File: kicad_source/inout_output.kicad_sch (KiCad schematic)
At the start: 8 parts

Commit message: started layout
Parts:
- gave numbers to parts that had none: 8
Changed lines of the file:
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@@
   (symbol (lib_id "power:GND") (at 85.09 71.12 0) (unit 1)
     (in_bom yes) (on_board yes) (fields_autoplaced)
-    (property "Reference" "#PWR?" (id 0) (at 85.09 77.47 0)
+    (property "Reference" "#PWR0124" (id 0) (at 85.09 77.47 0)
       (effects (font (size 1.27 1.27)) hide)
     )
@@
   (symbol (lib_id "power:GND") (at 140.97 113.03 0) (unit 1)
     (in_bom yes) (on_board yes) (fields_autoplaced)
-    (property "Reference" "#PWR?" (id 0) (at 140.97 119.38 0)
+    (property "Reference" "#PWR0133" (id 0) (at 140.97 119.38 0)
       (effects (font (size 1.27 1.27)) hide)
     )
@@
   (symbol (lib_id "power:GND") (at 119.38 97.79 0) (unit 1)
     (in_bom yes) (on_board yes) (fields_autoplaced)
-    (property "Reference" "#PWR?" (id 0) (at 119.38 104.14 0)
+    (property "Reference" "#PWR0131" (id 0) (at 119.38 104.14 0)
       (effects (font (size 1.27 1.27)) hide)
     )
@@
   (symbol (lib_id "power:GND") (at 119.38 52.07 0) (unit 1)
     (in_bom yes) (on_board yes) (fields_autoplaced)
-    (property "Reference" "#PWR?" (id 0) (at 119.38 58.42 0)
+    (property "Reference" "#PWR0129" (id 0) (at 119.38 58.42 0)
       (effects (font (size 1.27 1.27)) hide)
     )
@@
   (symbol (lib_id "power:GND") (at 140.97 67.31 0) (unit 1)
     (in_bom yes) (on_board yes) (fields_autoplaced)
-    (property "Reference" "#PWR?" (id 0) (at 140.97 73.66 0)
+    (property "Reference" "#PWR0132" (id 0) (at 140.97 73.66 0)
       (effects (font (size 1.27 1.27)) hide)
     )
@@
   (symbol (lib_id "power:+BATT") (at 119.38 43.18 0) (unit 1)
     (in_bom yes) (on_board yes) (fields_autoplaced)
-    (property "Reference" "#PWR?" (id 0) (at 119.38 46.99 0)
+    (property "Reference" "#PWR0128" (id 0) (at 119.38 46.99 0)
       (effects (font (size 1.27 1.27)) hide)
     )
@@
   (symbol (lib_id "Device:R_Small") (at 85.09 67.31 0) (unit 1)
     (in_bom yes) (on_board yes) (fields_autoplaced)
-    (property "Reference" "R?" (id 0) (at 87.63 66.0399 0)
+    (property "Reference" "R46" (id 0) (at 87.63 66.0399 0)
       (effects (font (size 1.27 1.27)) (justify left))
     )
@@
   (symbol (lib_id "generationmake:ITS4200S-ME-P") (at 105.41 107.95 0) (unit 1)
     (in_bom yes) (on_board yes) (fields_autoplaced)
-    (property "Reference" "U?" (id 0) (at 106.045 96.52 0))
+    (property "Reference" "U15" (id 0) (at 106.045 96.52 0))
     (property "Value" "ITS4200S-ME-P" (id 1) (at 106.045 99.06 0))
     (property "Footprint" "Package_TO_SOT_SMD:SOT-223" (id 2) (at 105.41 107.95 0)
@@
   (symbol (lib_id "generationmake:ITS4200S-ME-P") (at 105.41 62.23 0) (unit 1)
     (in_bom yes) (on_board yes) (fields_autoplaced)
-    (property "Reference" "U?" (id 0) (at 106.045 50.8 0))
+    (property "Reference" "U14" (id 0) (at 106.045 50.8 0))
     (property "Value" "ITS4200S-ME-P" (id 1) (at 106.045 53.34 0))
     (property "Footprint" "Package_TO_SOT_SMD:SOT-223" (id 2) (at 105.41 62.23 0)
@@
   (symbol (lib_id "Device:R_Small") (at 85.09 113.03 0) (unit 1)
     (in_bom yes) (on_board yes) (fields_autoplaced)
-    (property "Reference" "R?" (id 0) (at 87.63 111.7599 0)
+    (property "Reference" "R47" (id 0) (at 87.63 111.7599 0)
       (effects (font (size 1.27 1.27)) (justify left))
     )
@@
   (symbol (lib_id "power:GND") (at 85.09 116.84 0) (unit 1)
     (in_bom yes) (on_board yes) (fields_autoplaced)
-    (property "Reference" "#PWR?" (id 0) (at 85.09 123.19 0)
+    (property "Reference" "#PWR0125" (id 0) (at 85.09 123.19 0)
       (effects (font (size 1.27 1.27)) hide)
     )
@@
   (symbol (lib_id "power:GND") (at 115.57 69.85 0) (unit 1)
     (in_bom yes) (on_board yes) (fields_autoplaced)
-    (property "Reference" "#PWR?" (id 0) (at 115.57 76.2 0)
+    (property "Reference" "#PWR0126" (id 0) (at 115.57 76.2 0)
       (effects (font (size 1.27 1.27)) hide)
     )
@@
   (symbol (lib_id "power:GND") (at 115.57 115.57 0) (unit 1)
     (in_bom yes) (on_board yes) (fields_autoplaced)
-    (property "Reference" "#PWR?" (id 0) (at 115.57 121.92 0)
+    (property "Reference" "#PWR0127" (id 0) (at 115.57 121.92 0)
       (effects (font (size 1.27 1.27)) hide)
     )
@@
   (symbol (lib_id "Device:C_Small") (at 119.38 48.26 0) (unit 1)
     (in_bom yes) (on_board yes) (fields_autoplaced)
-    (property "Reference" "C?" (id 0) (at 121.92 46.9962 0)
+    (property "Reference" "C46" (id 0) (at 121.92 46.9962 0)
       (effects (font (size 1.27 1.27)) (justify left))
     )
@@
   (symbol (lib_id "Connector_Generic:Conn_01x02") (at 148.59 107.95 0) (unit 1)
     (in_bom yes) (on_board yes) (fields_autoplaced)
-    (property "Reference" "J?" (id 0) (at 151.13 107.9499 0)
+    (property "Reference" "J14" (id 0) (at 151.13 107.9499 0)
       (effects (font (size 1.27 1.27)) (justify left))
     )
@@
   (symbol (lib_id "power:+BATT") (at 119.38 88.9 0) (unit 1)
     (in_bom yes) (on_board yes) (fields_autoplaced)
-    (property "Reference" "#PWR?" (id 0) (at 119.38 92.71 0)
+    (property "Reference" "#PWR0130" (id 0) (at 119.38 92.71 0)
       (effects (font (size 1.27 1.27)) hide)
     )
@@
   (symbol (lib_id "Connector_Generic:Conn_01x02") (at 148.59 62.23 0) (unit 1)
     (in_bom yes) (on_board yes) (fields_autoplaced)
-    (property "Reference" "J?" (id 0) (at 151.13 62.2299 0)
+    (property "Reference" "J13" (id 0) (at 151.13 62.2299 0)
       (effects (font (size 1.27 1.27)) (justify left))
     )
@@
   (symbol (lib_id "Device:C_Small") (at 119.38 93.98 0) (unit 1)
     (in_bom yes) (on_board yes) (fields_autoplaced)
-    (property "Reference" "C?" (id 0) (at 121.92 92.7162 0)
-      (effects (font (size 1.27 1.27)) (justify left))
-    )
+    (property "Reference" "C47" (id 0) (at 121.92 92.7162 0)
+      (effects (font (size 1.27 1.27)) (justify left))
+    )

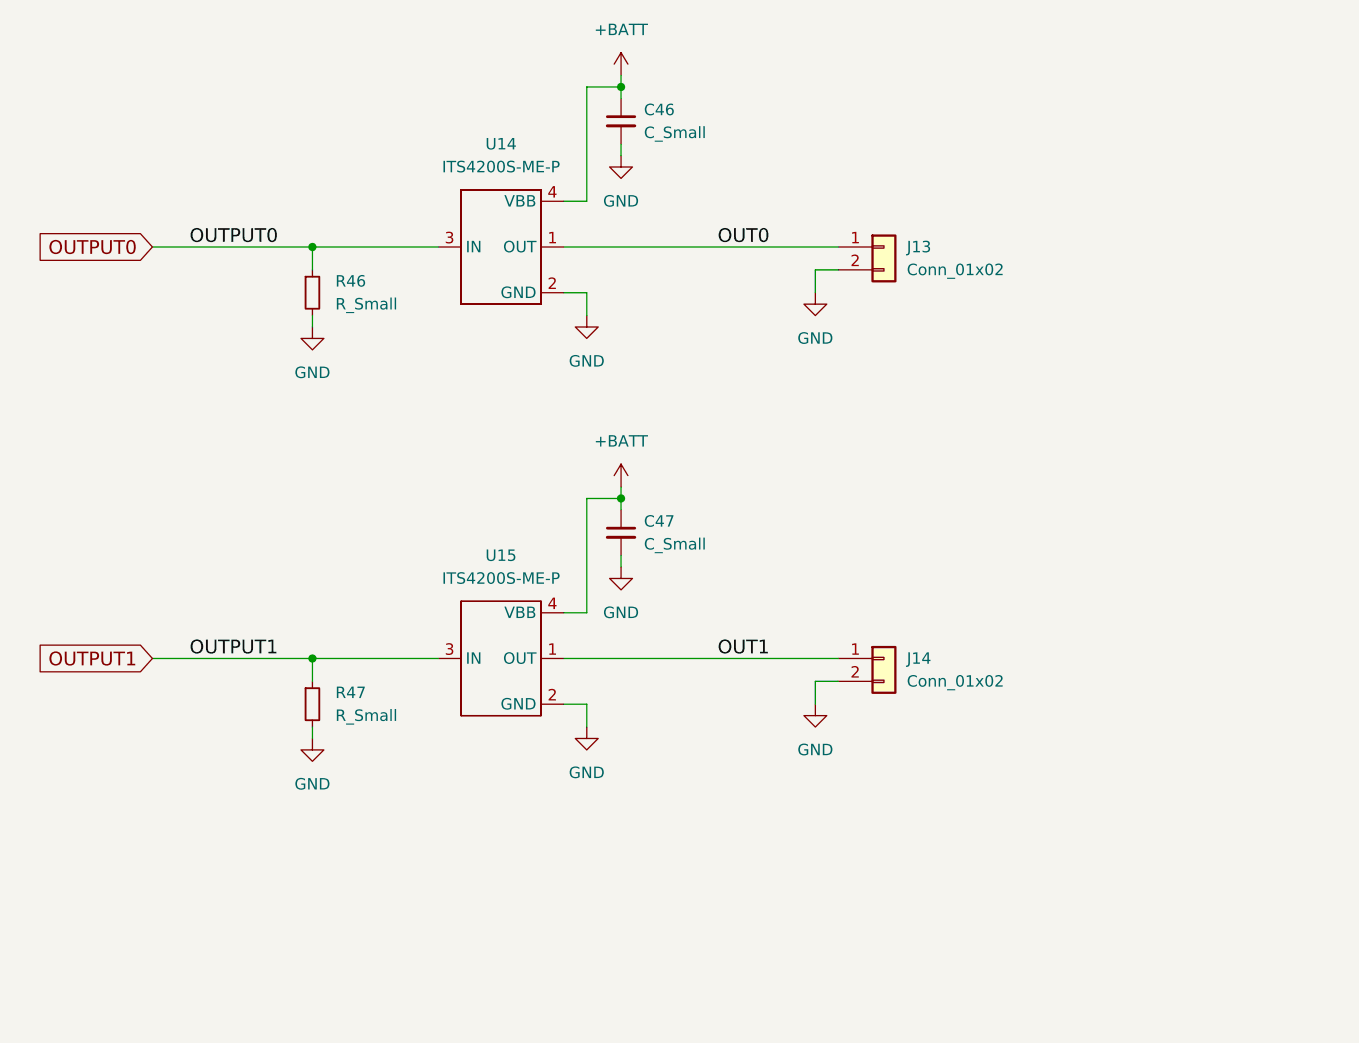
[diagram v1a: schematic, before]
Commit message: updated schematic pdf
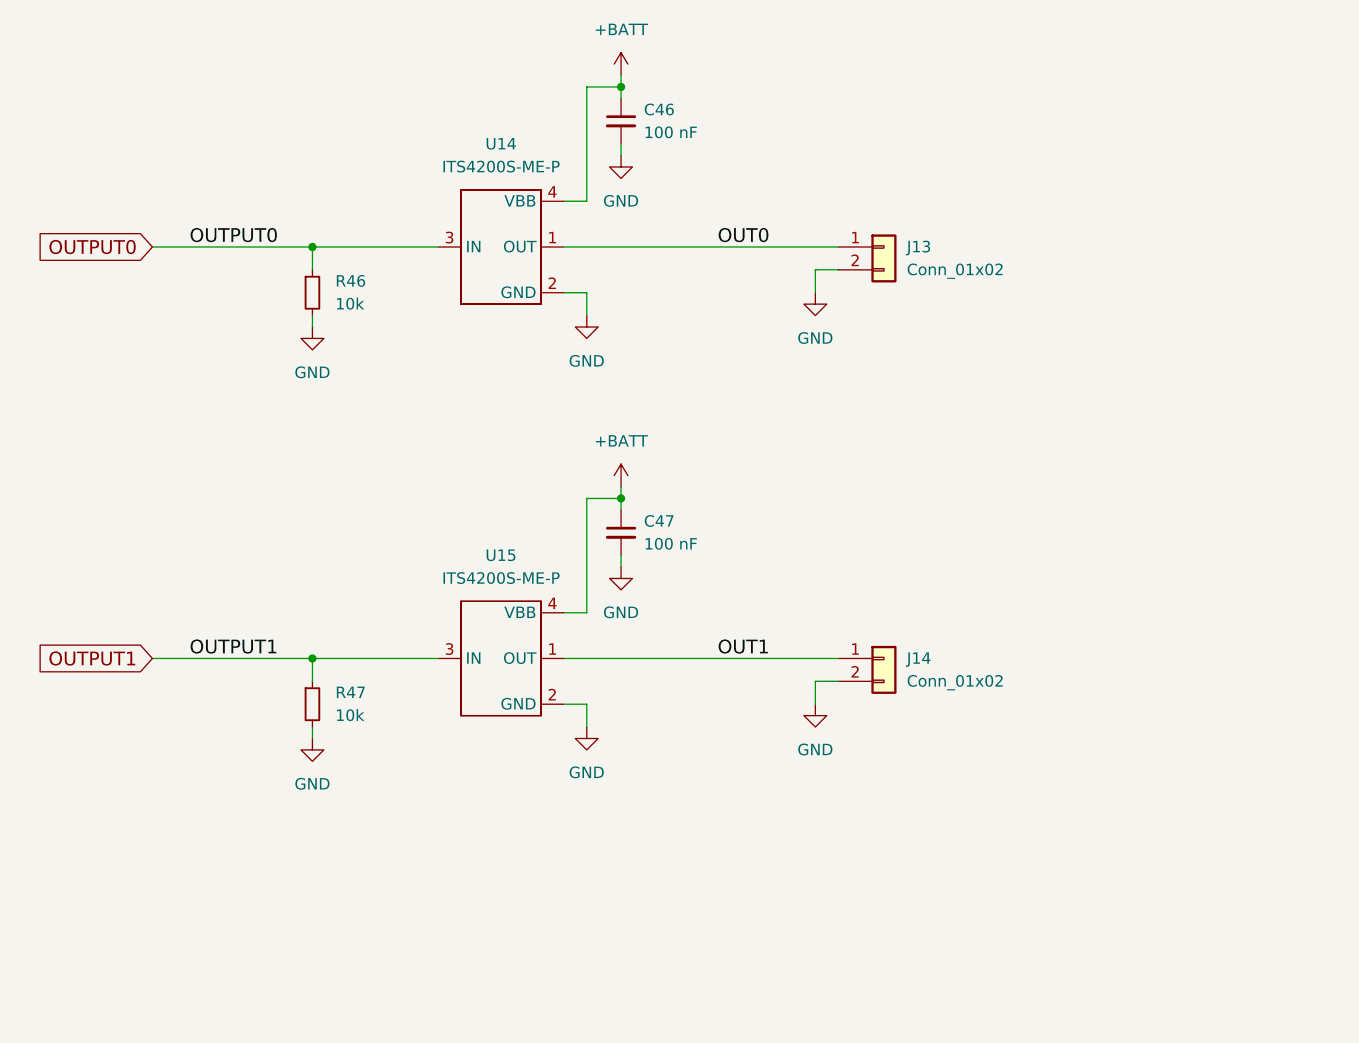
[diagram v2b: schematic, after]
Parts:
- C46, C47: value C_Small -> 100 nF
- R46, R47: value R_Small -> 10k
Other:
- company: (none) -> generationmake
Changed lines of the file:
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@@
   (title_block
     (title "CyphalRobotController07/CAN")
-    (date "2023-10-01")
+    (date "2023-10-02")
     (rev "0.1")
+    (company "generationmake")
   )
   (junction (at 85.09 62.23) (diameter 0) (color 0 0 0 0)
@@
       (effects (font (size 1.27 1.27)) (justify left))
     )
-    (property "Value" "R_Small" (id 1) (at 87.63 68.5799 0)
+    (property "Value" "10k" (id 1) (at 87.63 68.5799 0)
       (effects (font (size 1.27 1.27)) (justify left))
     )
@@
       (effects (font (size 1.27 1.27)) (justify left))
     )
-    (property "Value" "R_Small" (id 1) (at 87.63 114.2999 0)
+    (property "Value" "10k" (id 1) (at 87.63 114.2999 0)
       (effects (font (size 1.27 1.27)) (justify left))
     )
@@
       (effects (font (size 1.27 1.27)) (justify left))
     )
-    (property "Value" "C_Small" (id 1) (at 121.92 49.5362 0)
+    (property "Value" "100 nF" (id 1) (at 121.92 49.5362 0)
       (effects (font (size 1.27 1.27)) (justify left))
     )
@@
       (effects (font (size 1.27 1.27)) (justify left))
     )
-    (property "Value" "C_Small" (id 1) (at 121.92 95.2562 0)
-      (effects (font (size 1.27 1.27)) (justify left))
-    )
+    (property "Value" "100 nF" (id 1) (at 121.92 95.2562 0)
+      (effects (font (size 1.27 1.27)) (justify left))
+    )

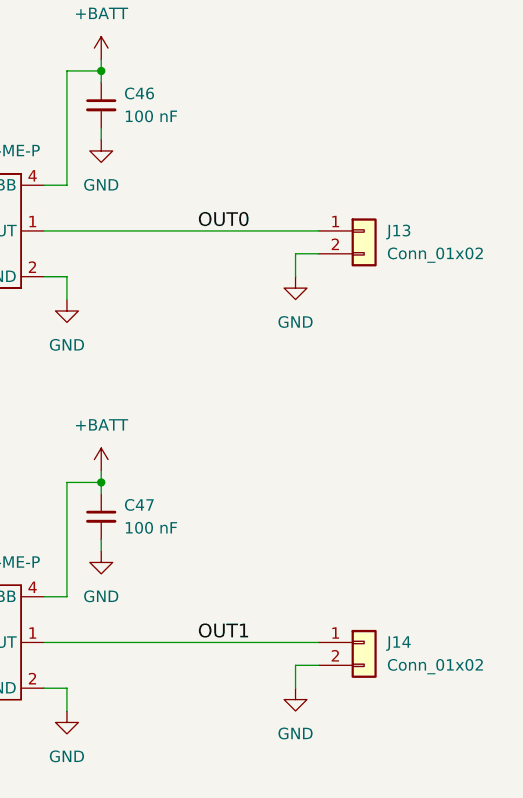
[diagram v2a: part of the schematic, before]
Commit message: updated 3d model to fit to reality
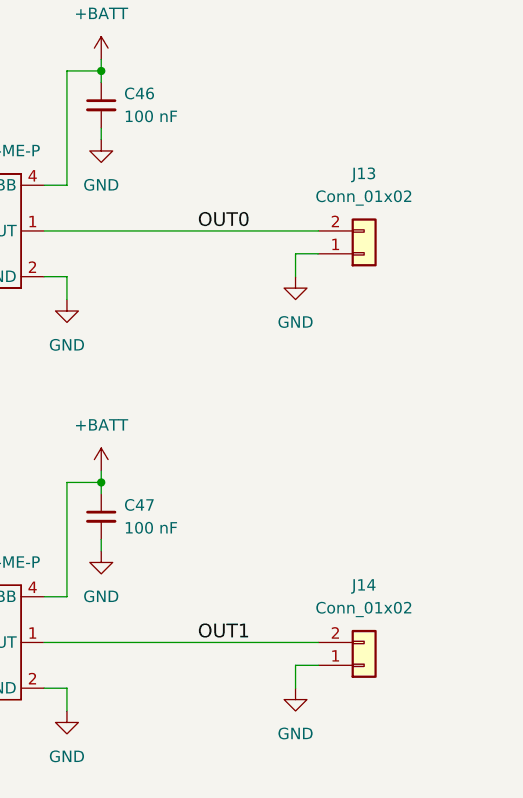
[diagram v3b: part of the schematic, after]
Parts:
- J13, J14: footprint Connector_Phoenix_MC:PhoenixContact_MCV_1,5_2-G-3.81_1x02_P3.81mm_Vertical -> Connector_Phoenix_MC:PhoenixContact_MC_1,5_2-G-3.81_1x02_P3.81mm_Horizontal
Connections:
- net GND: now also J13.1 (Pin_1), J14.1 (Pin_1); no longer J13.2 (Pin_2), J14.2 (Pin_2)
- net OUT0: now also J13.2 (Pin_2); no longer J13.1 (Pin_1)
- net OUT1: now also J14.2 (Pin_2); no longer J14.1 (Pin_1)
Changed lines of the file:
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@@
   (title_block
     (title "CyphalRobotController07/CAN")
-    (date "2023-10-02")
+    (date "2023-11-15")
     (rev "0.1")
     (company "generationmake")
@@
     (pin "2")
   )
-  (symbol (lib_id "Connector_Generic:Conn_01x02") (at 148.59 107.95 0) (unit 1)
-    (in_bom yes) (on_board yes) (fields_autoplaced)
-    (property "Reference" "J14" (id 0) (at 151.13 107.9499 0)
-      (effects (font (size 1.27 1.27)) (justify left))
-    )
-    (property "Value" "Conn_01x02" (id 1) (at 151.13 110.4899 0)
-      (effects (font (size 1.27 1.27)) (justify left))
-    )
-    (property "Footprint" "Connector_Phoenix_MC:PhoenixContact_MCV_1,5_2-G-3.81_1x02_P3.81mm_Vertical" (id 2) (at 148.59 107.95 0)
-      (effects (font (size 1.27 1.27)) hide)
-    )
-    (property "Datasheet" "~" (id 3) (at 148.59 107.95 0)
+  (symbol (lib_id "Connector_Generic:Conn_01x02") (at 148.59 110.49 0) (mirror x) (unit 1)
+    (in_bom yes) (on_board yes) (fields_autoplaced)
+    (property "Reference" "J14" (id 0) (at 148.59 101.6 0))
+    (property "Value" "Conn_01x02" (id 1) (at 148.59 104.14 0))
+    (property "Footprint" "Connector_Phoenix_MC:PhoenixContact_MC_1,5_2-G-3.81_1x02_P3.81mm_Horizontal" (id 2) (at 148.59 110.49 0)
+      (effects (font (size 1.27 1.27)) hide)
+    )
+    (property "Datasheet" "~" (id 3) (at 148.59 110.49 0)
       (effects (font (size 1.27 1.27)) hide)
     )
@@
     (pin "1")
   )
-  (symbol (lib_id "Connector_Generic:Conn_01x02") (at 148.59 62.23 0) (unit 1)
-    (in_bom yes) (on_board yes) (fields_autoplaced)
-    (property "Reference" "J13" (id 0) (at 151.13 62.2299 0)
-      (effects (font (size 1.27 1.27)) (justify left))
-    )
-    (property "Value" "Conn_01x02" (id 1) (at 151.13 64.7699 0)
-      (effects (font (size 1.27 1.27)) (justify left))
-    )
-    (property "Footprint" "Connector_Phoenix_MC:PhoenixContact_MCV_1,5_2-G-3.81_1x02_P3.81mm_Vertical" (id 2) (at 148.59 62.23 0)
-      (effects (font (size 1.27 1.27)) hide)
-    )
-    (property "Datasheet" "~" (id 3) (at 148.59 62.23 0)
-      (effects (font (size 1.27 1.27)) hide)
-    )
+  (symbol (lib_id "Connector_Generic:Conn_01x02") (at 148.59 64.77 0) (mirror x) (unit 1)
+    (in_bom yes) (on_board yes) (fields_autoplaced)
+    (property "Reference" "J13" (id 0) (at 148.59 55.88 0))
+    (property "Value" "Conn_01x02" (id 1) (at 148.59 58.42 0))
+    (property "Footprint" "Connector_Phoenix_MC:PhoenixContact_MC_1,5_2-G-3.81_1x02_P3.81mm_Horizontal" (id 2) (at 148.59 64.77 0)
+      (effects (font (size 1.27 1.27)) hide)
+    )
+    (property "Datasheet" "~" (id 3) (at 148.59 64.77 0)
+      (effects (font (size 1.27 1.27)) hide)
+    )

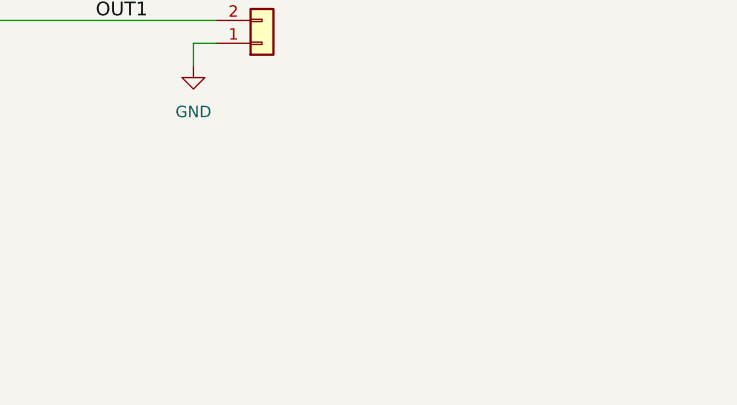
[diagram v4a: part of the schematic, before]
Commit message: added always on connector for +BATT
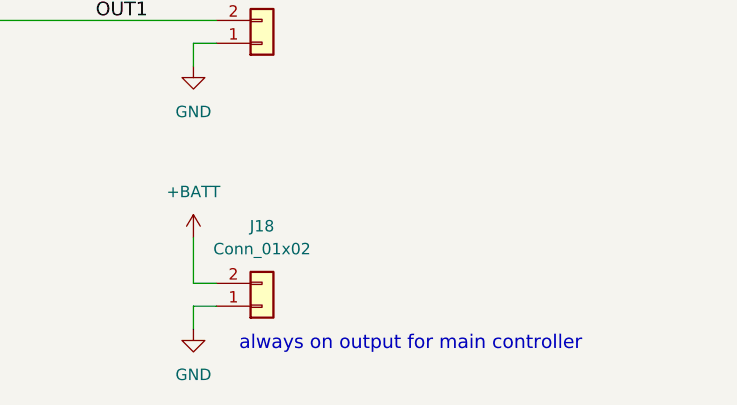
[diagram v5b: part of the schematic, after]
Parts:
- added J18: Conn_01x02, Connector_Phoenix_MC:PhoenixContact_MC_1,5_2-G-3.81_1x02_P3.81mm_Horizontal, symbol Connector_Generic:Conn_01x02
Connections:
- net +BATT: now also J18.2 (Pin_2)
- net GND: now also J18.1 (Pin_1)
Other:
- note added: "always on output for main controller"
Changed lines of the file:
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@@
+    (stroke (width 0) (type default) (color 0 0 0 0))
+  )
+  (wire (pts (xy 140.97 137.16) (xy 143.51 137.16))
     (stroke (width 0) (type default) (color 0 0 0 0))
   )
@@
     (stroke (width 0) (type default) (color 0 0 0 0))
   )
+  (wire (pts (xy 140.97 132.08) (xy 140.97 137.16))
+    (stroke (width 0) (type default) (color 0 0 0 0))
+  )
   (wire (pts (xy 67.31 62.23) (xy 85.09 62.23))
     (stroke (width 0) (type default) (color 0 0 0 0))
@@
     (stroke (width 0) (type default) (color 0 0 0 0))
   )
+  (wire (pts (xy 143.51 139.7) (xy 140.97 139.7))
+    (stroke (width 0) (type default) (color 0 0 0 0))
+  )
   (wire (pts (xy 115.57 57.15) (xy 115.57 44.45))
     (stroke (width 0) (type default) (color 0 0 0 0))
@@
     (stroke (width 0) (type default) (color 0 0 0 0))
   )
+  (wire (pts (xy 140.97 139.7) (xy 140.97 142.24))
+    (stroke (width 0) (type default) (color 0 0 0 0))
+  )
   (wire (pts (xy 119.38 88.9) (xy 119.38 90.17))
     (stroke (width 0) (type default) (color 0 0 0 0))
@@
   (wire (pts (xy 113.03 102.87) (xy 115.57 102.87))
     (stroke (width 0) (type default) (color 0 0 0 0))
+  )
+  (text "always on output for main controller" (at 146.05 144.78 0)
+    (effects (font (size 1.524 1.524)) (justify left bottom))
   )
   (label "OUT1" (at 135.89 107.95 180)
@@
     )
   )
+  (symbol (lib_id "power:+BATT") (at 140.97 132.08 0) (unit 1)
+    (in_bom yes) (on_board yes) (fields_autoplaced)
+    (property "Reference" "#PWR0160" (id 0) (at 140.97 135.89 0)
+      (effects (font (size 1.27 1.27)) hide)
+    )
+    (property "Value" "+BATT" (id 1) (at 140.97 127 0))
+    (property "Footprint" "" (id 2) (at 140.97 132.08 0)
+      (effects (font (size 1.27 1.27)) hide)
+    )
+    (property "Datasheet" "" (id 3) (at 140.97 132.08 0)
+      (effects (font (size 1.27 1.27)) hide)
+    )
+    (pin "1")
+  )
   (symbol (lib_id "power:GND") (at 85.09 71.12 0) (unit 1)
     (in_bom yes) (on_board yes) (fields_autoplaced)
@@
     (pin "1")
   )
+  (symbol (lib_id "power:GND") (at 140.97 142.24 0) (unit 1)
+    (in_bom yes) (on_board yes) (fields_autoplaced)
+    (property "Reference" "#PWR0161" (id 0) (at 140.97 148.59 0)
+      (effects (font (size 1.27 1.27)) hide)
+    )
+    (property "Value" "GND" (id 1) (at 140.97 147.32 0))
+    (property "Footprint" "" (id 2) (at 140.97 142.24 0)
+      (effects (font (size 1.27 1.27)) hide)
+    )
+    (property "Datasheet" "" (id 3) (at 140.97 142.24 0)
+      (effects (font (size 1.27 1.27)) hide)
+    )
+    (pin "1")
+  )
+  (symbol (lib_id "Connector_Generic:Conn_01x02") (at 148.59 139.7 0) (mirror x) (unit 1)
+    (in_bom yes) (on_board yes) (fields_autoplaced)
+    (property "Reference" "J18" (id 0) (at 148.59 130.81 0))
+    (property "Value" "Conn_01x02" (id 1) (at 148.59 133.35 0))
+    (property "Footprint" "Connector_Phoenix_MC:PhoenixContact_MC_1,5_2-G-3.81_1x02_P3.81mm_Horizontal" (id 2) (at 148.59 139.7 0)
+      (effects (font (size 1.27 1.27)) hide)
+    )
+    (property "Datasheet" "~" (id 3) (at 148.59 139.7 0)
+      (effects (font (size 1.27 1.27)) hide)
+    )
+    (pin "1")
+    (pin "2")
+  )
   (symbol (lib_id "Device:R_Small") (at 85.09 67.31 0) (unit 1)
